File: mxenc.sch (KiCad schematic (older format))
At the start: 33 parts, among them J4 Conn_01x06, J6 Conn_01x06, J8 Conn_01x04_MountingPin, SW1 SW_Push, SW2 SW_Push, U1 IMX8MM, U10 24C32, Y2 Crystal_GND24

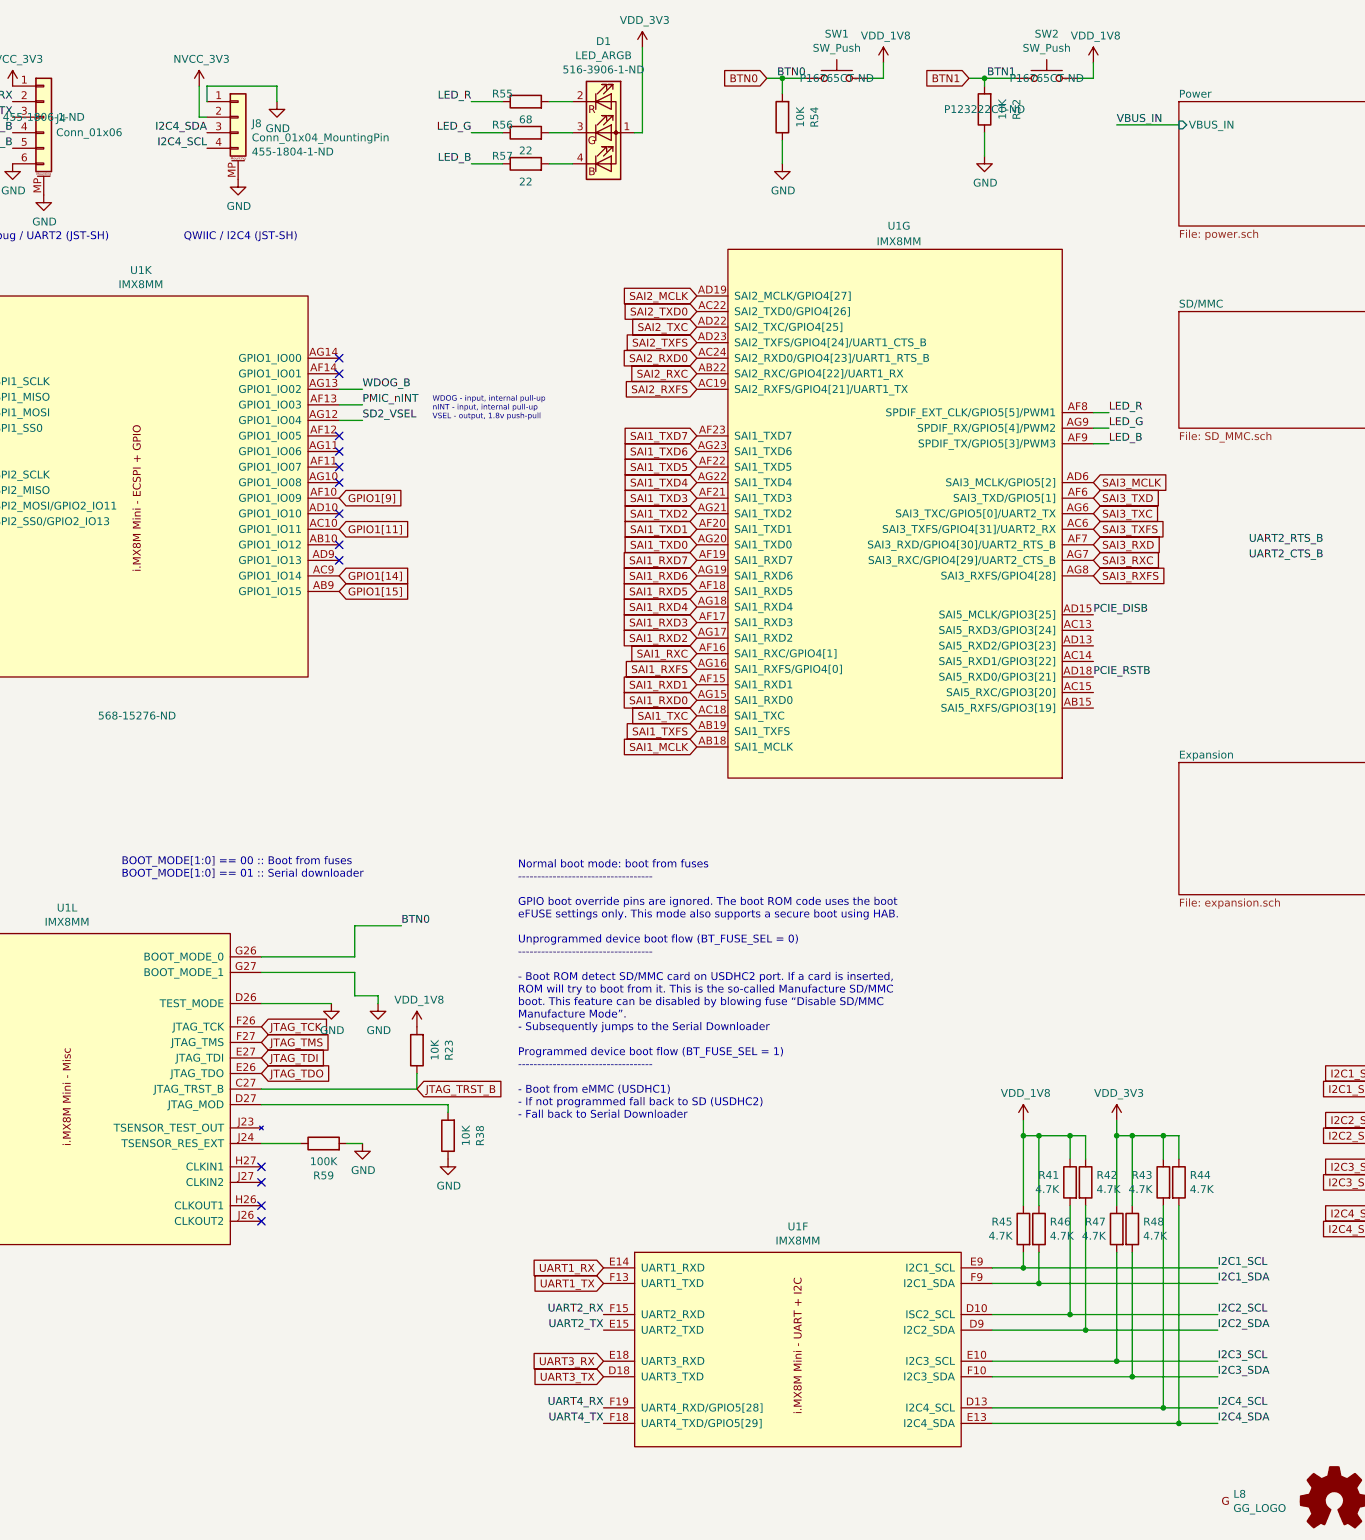
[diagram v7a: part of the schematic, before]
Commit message: Change expansion audio routing to sai2/3
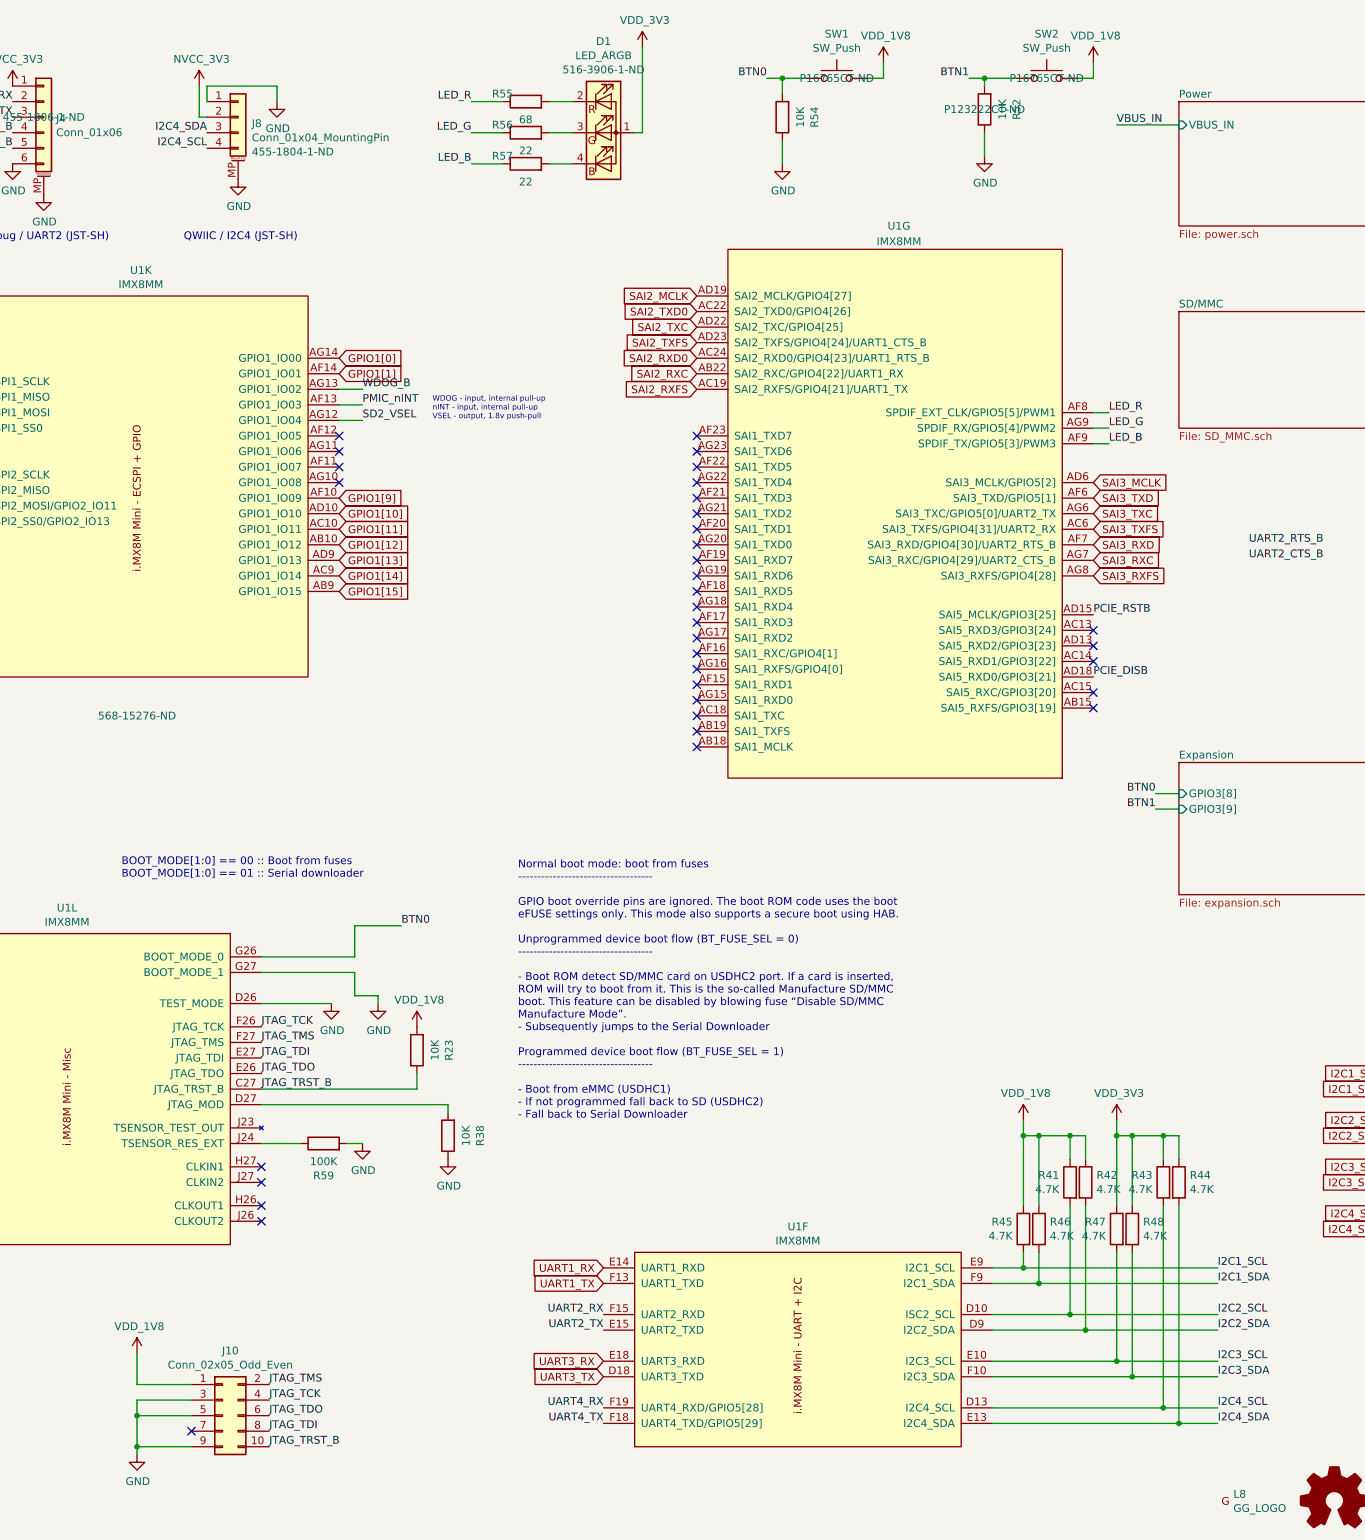
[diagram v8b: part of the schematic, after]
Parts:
- added J10: Conn_02x05_Odd_Even, Connector_PinHeader_1.27mm:PinHeader_2x05_P1.27mm_Vertical_SMD, symbol Connector_Generic:Conn_02x05_Odd_Even
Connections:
- net GND: now also J10.3 (Pin_3), J10.5 (Pin_5), J10.9 (Pin_9)
- net JTAG_TCK: now also J10.4 (Pin_4)
- net JTAG_TDI: now also J10.8 (Pin_8)
- net JTAG_TDO: now also J10.6 (Pin_6)
- net JTAG_TMS: now also J10.2 (Pin_2)
- net JTAG_TRST_B: now also J10.10 (Pin_10)
- net PCIE_DISB: now also U1.AD18 (SAI5_RXD0/GPIO3[21]); no longer U1.AD15 (SAI5_MCLK/GPIO3[25])
- net PCIE_RSTB: now also U1.AD15 (SAI5_MCLK/GPIO3[25]); no longer U1.AD18 (SAI5_RXD0/GPIO3[21])
- net VDD_1V8: now also J10.1 (Pin_1)
- net GPIO1[12]: now reaches U1.AB10 (GPIO1_IO12)
- net GPIO1[10]: now reaches U1.AD10 (GPIO1_IO10)
- net GPIO1[13]: now reaches U1.AD9 (GPIO1_IO13)
- net GPIO1[1]: now reaches U1.AF14 (GPIO1_IO01)
- net GPIO1[0]: now reaches U1.AG14 (GPIO1_IO00)
- net SAI1_MCLK: no longer names the net of U1.AB18 (SAI1_MCLK)
- net SAI1_RXC: no longer names the net of U1.AF16 (SAI1_RXC/GPIO4[1])
- net SAI1_RXD0: no longer names the net of U1.AG15 (SAI1_RXD0)
- net SAI1_RXD1: no longer names the net of U1.AF15 (SAI1_RXD1)
- net SAI1_RXD2: no longer names the net of U1.AG17 (SAI1_RXD2)
- net SAI1_RXD3: no longer names the net of U1.AF17 (SAI1_RXD3)
- net SAI1_RXD4: no longer names the net of U1.AG18 (SAI1_RXD4)
- net SAI1_RXD5: no longer names the net of U1.AF18 (SAI1_RXD5)
- net SAI1_RXD6: no longer names the net of U1.AG19 (SAI1_RXD6)
- net SAI1_RXD7: no longer names the net of U1.AF19 (SAI1_RXD7)
- net SAI1_RXFS: no longer names the net of U1.AG16 (SAI1_RXFS/GPIO4[0])
- net SAI1_TXC: no longer names the net of U1.AC18 (SAI1_TXC)
- net SAI1_TXD0: no longer names the net of U1.AG20 (SAI1_TXD0)
- net SAI1_TXD1: no longer names the net of U1.AF20 (SAI1_TXD1)
- net SAI1_TXD2: no longer names the net of U1.AG21 (SAI1_TXD2)
- net SAI1_TXD3: no longer names the net of U1.AF21 (SAI1_TXD3)
- net SAI1_TXD4: no longer names the net of U1.AG22 (SAI1_TXD4)
- net SAI1_TXD5: no longer names the net of U1.AF22 (SAI1_TXD5)
- net SAI1_TXD6: no longer names the net of U1.AG23 (SAI1_TXD6)
- net SAI1_TXD7: no longer names the net of U1.AF23 (SAI1_TXD7)
- net SAI1_TXFS: no longer names the net of U1.AB19 (SAI1_TXFS)
- no-connect marks 13 -> 35
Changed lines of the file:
@@
 Wire Wire Line
 	8450 1700 8450 1550
-Text Label 8600 1150 2    50   ~ 0
+Text Label 8350 1150 2    50   ~ 0
 BTN0
 $Comp
@@
 NoConn ~ 5600 3550
 NoConn ~ 5600 3650
-NoConn ~ 5600 3950
-NoConn ~ 5600 4150
-NoConn ~ 5600 4250
 Wire Wire Line
 	2000 1200 2050 1200
@@
 Wire Wire Line
 	13000 6200 13350 6200
-Text Label 10450 5000 0    50   ~ 0
+Text Label 10450 4600 0    50   ~ 0
 PCIE_RSTB
-Text Label 10450 4600 0    50   ~ 0
-PCIE_DISB
 Text Label 13100 6850 2    50   ~ 0
 TCPC_~INT
@@
 F0 "Expansion" 50
 F1 "expansion.sch" 50
+F2 "GPIO3[8]" I L 11000 5750 50
+F3 "GPIO3[9]" I L 11000 5850 50
 $EndSheet
 Wire Wire Line
 	5550 7100 5100 7100
-Text GLabel 5100 7250 2    50   Input ~ 0
-JTAG_TCK
-Text GLabel 5100 7350 2    50   Input ~ 0
-JTAG_TMS
-Text GLabel 5100 7450 2    50   Input ~ 0
-JTAG_TDI
-Text GLabel 5100 7550 2    50   Input ~ 0
-JTAG_TDO
-Text GLabel 6100 7650 2    50   Input ~ 0
-JTAG_TRST_B
 Wire Wire Line
 	8350 1150 8450 1150
@@
 Wire Wire Line
 	9750 1650 9750 1500
-Text Label 9950 1150 2    50   ~ 0
+Text Label 9650 1150 2    50   ~ 0
 BTN1
 Wire Wire Line
@@
 	1    0    0    -1
 $EndComp
-Text GLabel 7900 3450 0    50   Input ~ 0
-SAI1_TXD7
-Text GLabel 7900 3550 0    50   Input ~ 0
-SAI1_TXD6
-Text GLabel 7900 3650 0    50   Input ~ 0
-SAI1_TXD5
-Text GLabel 7900 3750 0    50   Input ~ 0
-SAI1_TXD4
-Text GLabel 7900 3850 0    50   Input ~ 0
-SAI1_TXD3
-Text GLabel 7900 3950 0    50   Input ~ 0
-SAI1_TXD2
-Text GLabel 7900 4050 0    50   Input ~ 0
-SAI1_TXD1
-Text GLabel 7900 4150 0    50   Input ~ 0
-SAI1_TXD0
-Text GLabel 7900 4250 0    50   Input ~ 0
-SAI1_RXD7
-Text GLabel 7900 4350 0    50   Input ~ 0
-SAI1_RXD6
-Text GLabel 7900 4450 0    50   Input ~ 0
-SAI1_RXD5
-Text GLabel 7900 4550 0    50   Input ~ 0
-SAI1_RXD4
-Text GLabel 7900 4650 0    50   Input ~ 0
-SAI1_RXD3
-Text GLabel 7900 4750 0    50   Input ~ 0
-SAI1_RXD2
-Text GLabel 7900 4850 0    50   Input ~ 0
-SAI1_RXC
-Text GLabel 7900 4950 0    50   Input ~ 0
-SAI1_RXFS
-Text GLabel 7900 5050 0    50   Input ~ 0
-SAI1_RXD1
-Text GLabel 7900 5150 0    50   Input ~ 0
-SAI1_RXD0
-Text GLabel 7900 5250 0    50   Input ~ 0
-SAI1_TXC
-Text GLabel 7900 5350 0    50   Input ~ 0
-SAI1_TXFS
-Text GLabel 7900 5450 0    50   Input ~ 0
-SAI1_MCLK
-Text GLabel 8350 1150 0    50   Input ~ 0
-BTN0
-Text GLabel 9650 1150 0    50   Input ~ 0
-BTN1
 Text GLabel 3050 3700 0    50   Input ~ 0
 ECSPI2_SCLK
@@
 Text Label 2550 4700 3    50   ~ 0
 UART4_RTS_B
-NoConn ~ 5600 2950
-NoConn ~ 5600 3050
 Text GLabel 10450 3750 2    50   Input ~ 0
 SAI3_MCLK
@@
 Text GLabel 7900 3150 0    50   Input ~ 0
 SAI2_RXFS
+Text GLabel 5600 2950 2    50   Input ~ 0
+GPIO1[0]
+Text GLabel 5600 3050 2    50   Input ~ 0
+GPIO1[1]
+Text GLabel 5600 3950 2    50   Input ~ 0
+GPIO1[10]
+Text GLabel 5600 4150 2    50   Input ~ 0
+GPIO1[12]
+Text GLabel 5600 4250 2    50   Input ~ 0
+GPIO1[13]
+Text Label 10450 5000 0    50   ~ 0
+PCIE_DISB
+NoConn ~ 7900 3450
+NoConn ~ 7900 3550
+NoConn ~ 7900 3650
+NoConn ~ 7900 3750
+NoConn ~ 7900 3850
+NoConn ~ 7900 3950
+NoConn ~ 7900 4050
+NoConn ~ 7900 4150
+NoConn ~ 7900 4250
+NoConn ~ 7900 4350
+NoConn ~ 7900 4450
+NoConn ~ 7900 4550
+NoConn ~ 7900 4650
+NoConn ~ 7900 4750
+NoConn ~ 7900 4850
+NoConn ~ 7900 4950
+NoConn ~ 7900 5050
+NoConn ~ 7900 5150
+NoConn ~ 7900 5250
+NoConn ~ 7900 5350
+NoConn ~ 7900 5450
+NoConn ~ 10450 4700
+NoConn ~ 10450 4800
+NoConn ~ 10450 4900
+NoConn ~ 10450 5100
+NoConn ~ 10450 5200
+Text Label 10850 5750 2    50   ~ 0
+BTN0
+Wire Wire Line
+	10850 5750 11000 5750
+Text Label 10850 5850 2    50   ~ 0
+BTN1
+Wire Wire Line
+	10850 5850 11000 5850
+$Comp
+L Connector_Generic:Conn_02x05_Odd_Even J?
+U 1 1 5F857066
+P 4850 9750
+AR Path="/5E34BAA5/5F857066" Ref="J?"  Part="1"
+AR Path="/5F857066" Ref="J10"  Part="1"
+F 0 "J10" H 4900 10167 50  0000 C CNN
+F 1 "Conn_02x05_Odd_Even" H 4900 10076 50  0000 C CNN
+F 2 "Connector_PinHeader_1.27mm:PinHeader_2x05_P1.27mm_Vertical_SMD" H 4850 9750 50  0001 C CNN
+F 3 "~" H 4850 9750 50  0001 C CNN
+	1    4850 9750
+	1    0    0    -1
+$EndComp
+$Comp
+L power:GND #PWR?
+U 1 1 5F85706C
+P 4300 10000
+AR Path="/5E34BAA5/5F85706C" Ref="#PWR?"  Part="1"
+AR Path="/5F85706C" Ref="#PWR0239"  Part="1"
+F 0 "#PWR0239" H 4300 9750 50  0001 C CNN
+F 1 "GND" H 4305 9827 50  0000 C CNN
+F 2 "" H 4300 10000 50  0001 C CNN
+F 3 "" H 4300 10000 50  0001 C CNN
+	1    4300 10000
+	1    0    0    -1
+$EndComp
+Wire Wire Line
+	4300 10000 4300 9950
+Wire Wire Line
+	4300 9750 4650 9750
+Wire Wire Line
+	4650 9650 4300 9650
+Wire Wire Line
+	4300 9650 4300 9750
+Connection ~ 4300 9750
+Wire Wire Line
+	4650 9950 4300 9950
+Connection ~ 4300 9950
+Wire Wire Line
+	4300 9950 4300 9750
+NoConn ~ 4650 9850
+$Comp
+L mxenc:VDD_1V8 #PWR?
+U 1 1 5F85707B
+P 4300 9350
+AR Path="/5E34BAA5/5F85707B" Ref="#PWR?"  Part="1"
+AR Path="/5F85707B" Ref="#PWR0244"  Part="1"
+F 0 "#PWR0244" H 4300 9200 50  0001 C CNN
+F 1 "VDD_1V8" H 4315 9523 50  0000 C CNN
+F 2 "" H 4300 9350 50  0001 C CNN
+F 3 "" H 4300 9350 50  0001 C CNN
+	1    4300 9350
+	1    0    0    -1
+$EndComp
+Wire Wire Line
+	4300 9350 4300 9550
+Wire Wire Line
+	4300 9550 4650 9550
+Text Label 5100 7250 0    50   ~ 0
+JTAG_TCK
+Text Label 5100 7350 0    50   ~ 0
+JTAG_TMS
+Text Label 5100 7450 0    50   ~ 0
+JTAG_TDI
+Text Label 5100 7550 0    50   ~ 0
+JTAG_TDO
+Text Label 5100 7650 0    50   ~ 0
+JTAG_TRST_B
+Text Label 5150 9650 0    50   ~ 0
+JTAG_TCK
+Text Label 5150 9550 0    50   ~ 0
+JTAG_TMS
+Text Label 5150 9850 0    50   ~ 0
+JTAG_TDI
+Text Label 5150 9750 0    50   ~ 0
+JTAG_TDO
+Text Label 5150 9950 0    50   ~ 0
+JTAG_TRST_B
 $EndSCHEMATC
